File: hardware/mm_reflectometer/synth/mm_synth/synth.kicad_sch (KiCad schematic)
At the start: 44 parts

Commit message: adding bias circuitry to mm synth
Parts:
- added C?: 100 nF, symbol Device:C_Small
- added R?: 47k, symbol Device:R_Small
- FB? (x6): value FerriteBead_Small -> BLM15GG471SZ1D
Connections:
- net GND: now also C?.1
- net at C?.1, R?.2: now also U?.14 (CPout)
- net at U?.43 (Vtune): now also R?.1, R?.2
- new net VT_UNBUF: C?.2, R?.1
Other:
- note added: "TODO: CHECK CURRENTS, MAX 200 MA/FERRITE"
- moved on the sheet: C?, R?

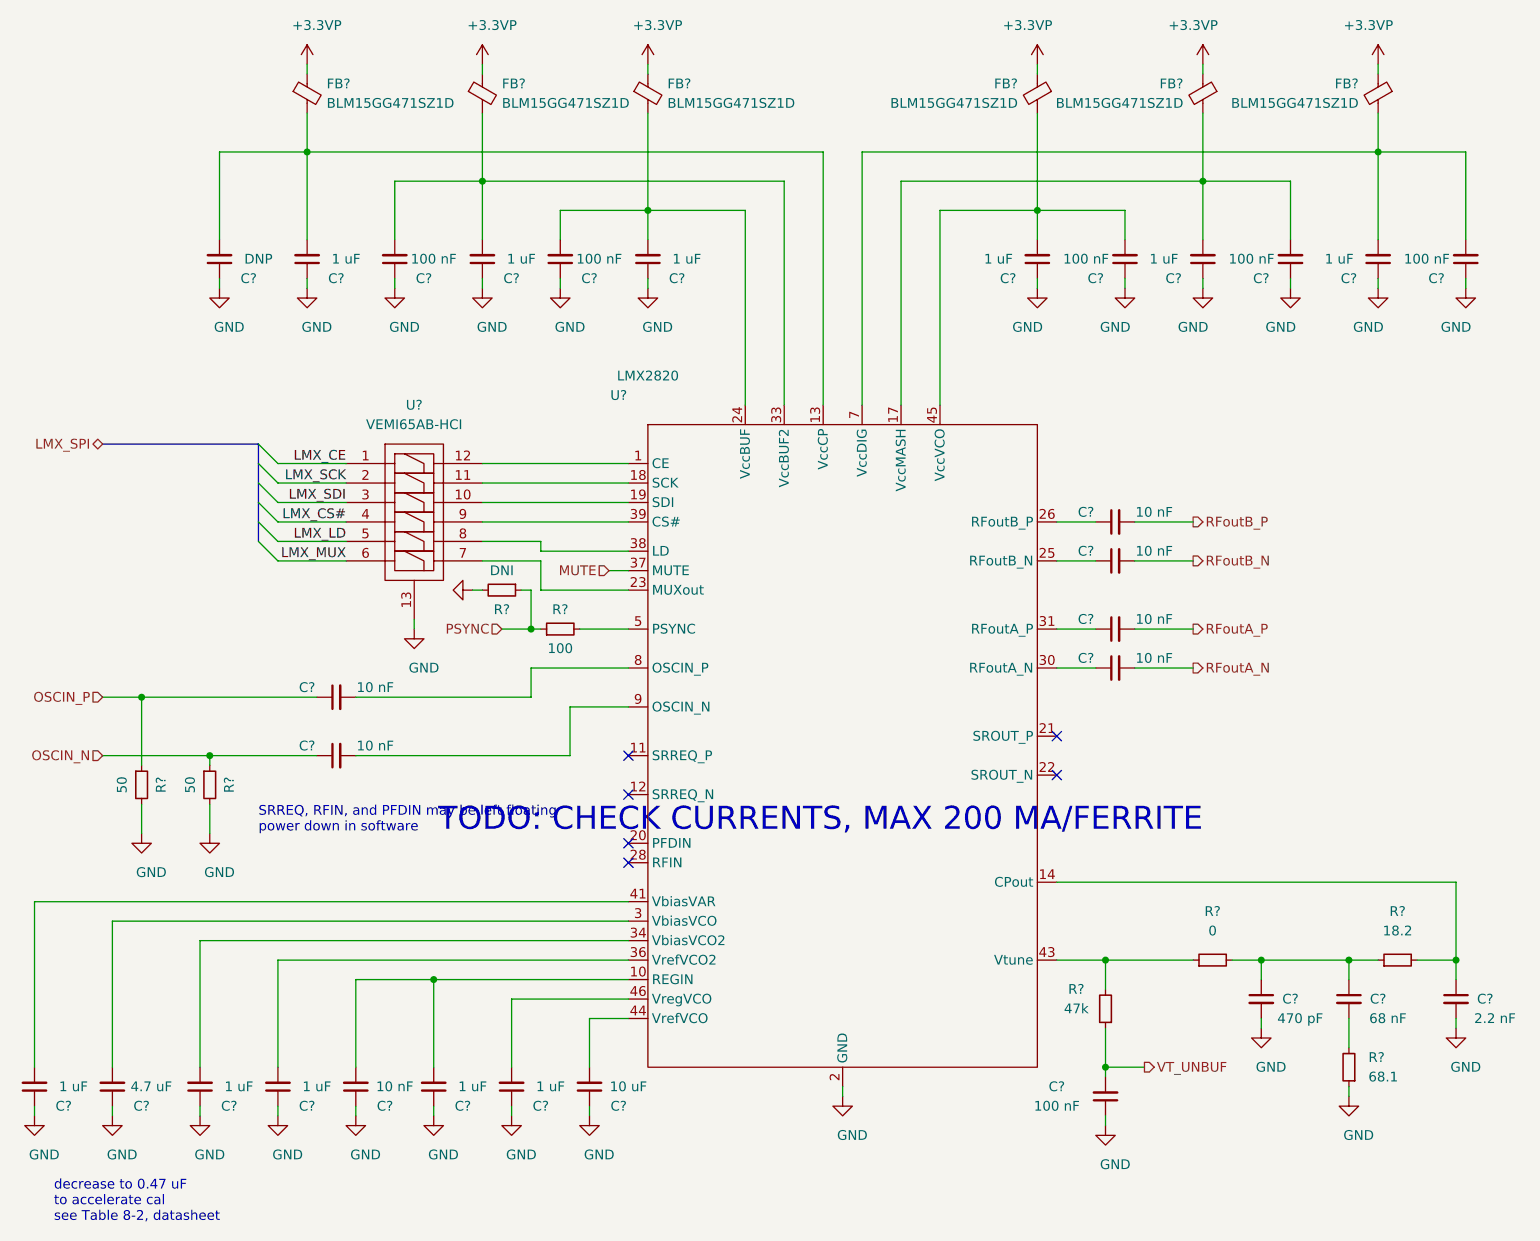
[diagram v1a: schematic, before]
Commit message: schematic work on mm synth -- starting voltage regulation
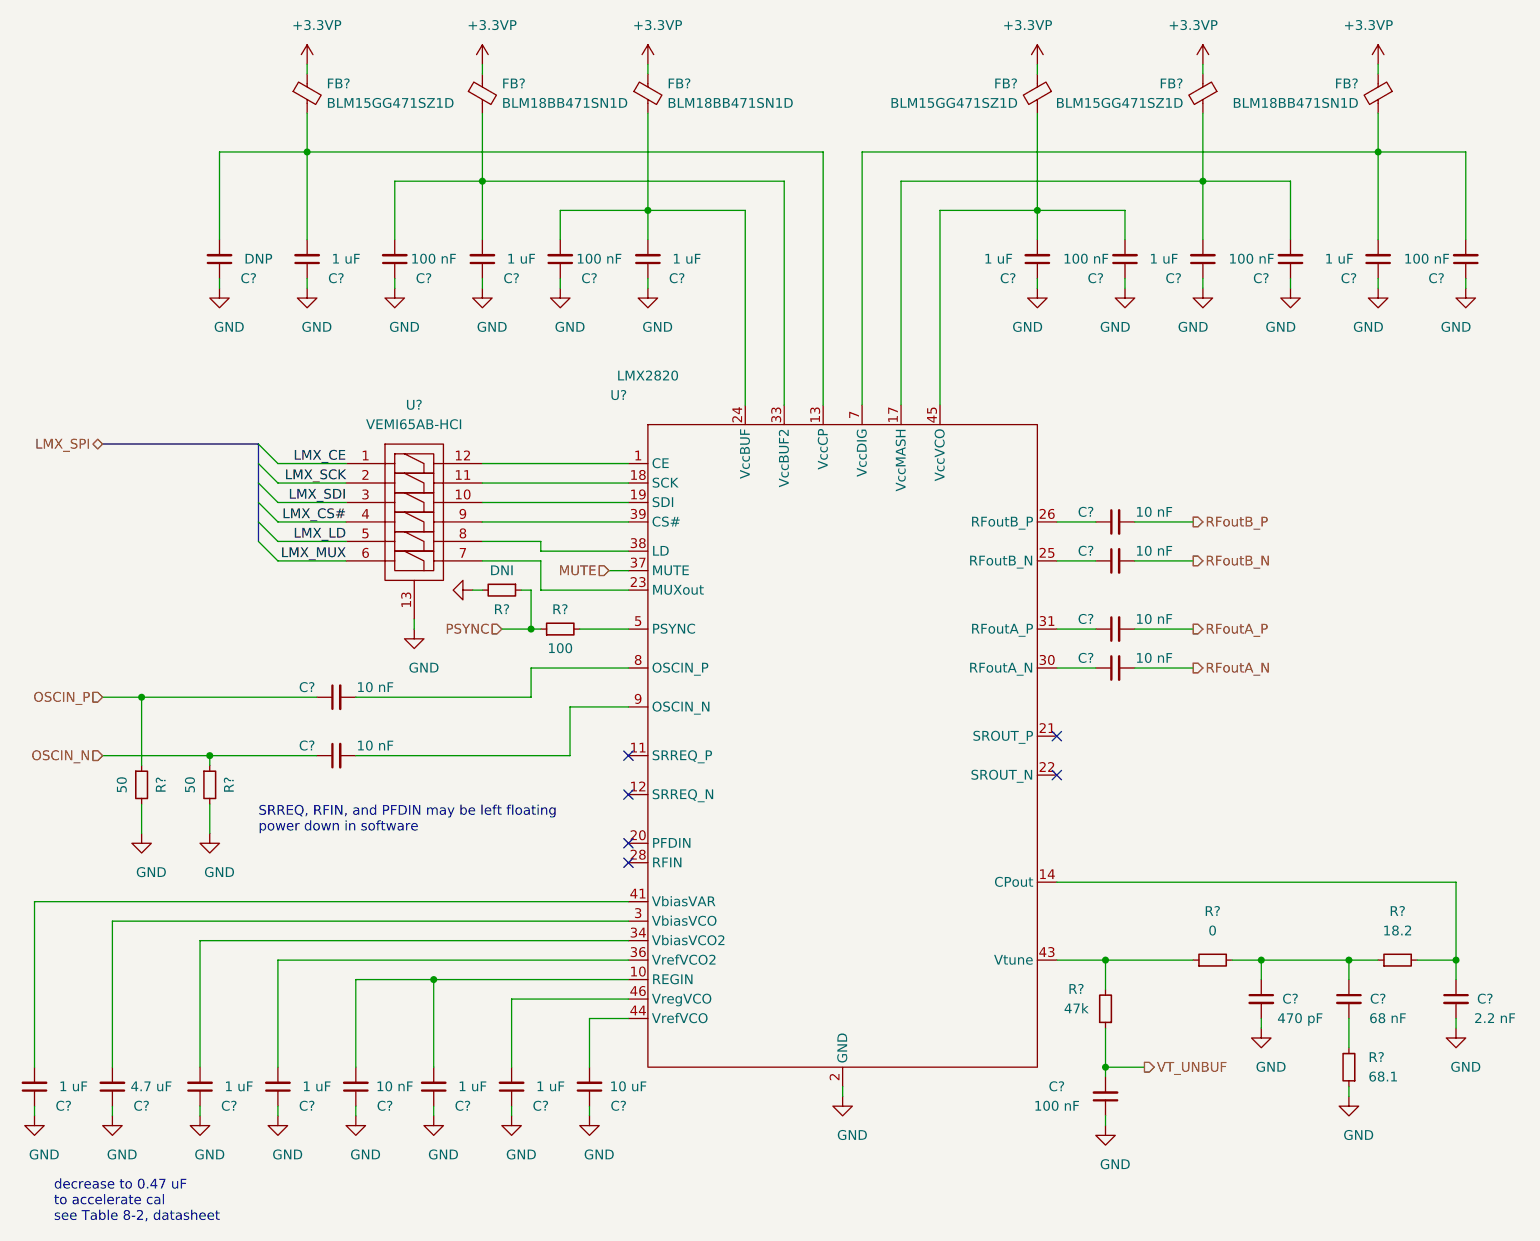
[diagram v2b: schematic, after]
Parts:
- FB? (x3): value BLM15GG471SZ1D -> BLM18BB471SN1D
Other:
- note removed: "TODO: CHECK CURRENTS, MAX 200 MA/FERRITE"
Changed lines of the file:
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@@
-(kicad_sch (version 20210126) (generator eeschema)
+(kicad_sch (version 20210406) (generator eeschema)
   (paper "A4")
   (junction (at 64.77 102.87) (diameter 0.9144) (color 0 0 0 0))
@@
     (stroke (width 0) (type solid) (color 0 0 0 0))
   )
-  (bus (pts (xy 80.01 72.39) (xy 80.01 69.85))
-    (stroke (width 0) (type solid) (color 0 0 0 0))
-  )
-  (bus (pts (xy 80.01 74.93) (xy 80.01 72.39))
-    (stroke (width 0) (type solid) (color 0 0 0 0))
-  )
-  (bus (pts (xy 80.01 77.47) (xy 80.01 74.93))
-    (stroke (width 0) (type solid) (color 0 0 0 0))
-  )
-  (bus (pts (xy 80.01 80.01) (xy 80.01 77.47))
-    (stroke (width 0) (type solid) (color 0 0 0 0))
-  )
-  (bus (pts (xy 80.01 82.55) (xy 80.01 80.01))
+  (bus (pts (xy 80.01 69.85) (xy 80.01 82.55))
     (stroke (width 0) (type solid) (color 0 0 0 0))
   )
@@
     (effects (font (size 1.27 1.27)) (justify left bottom))
   )
-  (text "TODO: CHECK CURRENTS, MAX 200 MA/FERRITE" (at 203.2 120.65 180)
-    (effects (font (size 3 3)) (justify right bottom))
-  )
   (label "LMX_CE" (at 91.44 72.39 180)
     (effects (font (size 1.27 1.27)) (justify right bottom))
@@
       (effects (font (size 1.27 1.27)) (justify left))
     )
-    (property "Value" "BLM15GG471SZ1D" (id 1) (at 111.76 25.4 0)
+    (property "Value" "BLM18BB471SN1D" (id 1) (at 111.76 25.4 0)
       (effects (font (size 1.27 1.27)) (justify left))
     )
@@
       (effects (font (size 1.27 1.27)) (justify left))
     )
-    (property "Value" "BLM15GG471SZ1D" (id 1) (at 133.35 25.4 0)
+    (property "Value" "BLM18BB471SN1D" (id 1) (at 133.35 25.4 0)
       (effects (font (size 1.27 1.27)) (justify left))
     )
@@
       (effects (font (size 1.27 1.27)) (justify left))
     )
-    (property "Value" "BLM15GG471SZ1D" (id 1) (at 223.52 25.4 0)
+    (property "Value" "BLM18BB471SN1D" (id 1) (at 223.52 25.4 0)
       (effects (font (size 1.27 1.27)) (justify left))
     )

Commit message: work on mm synth schematic - control signals and footprint assignments
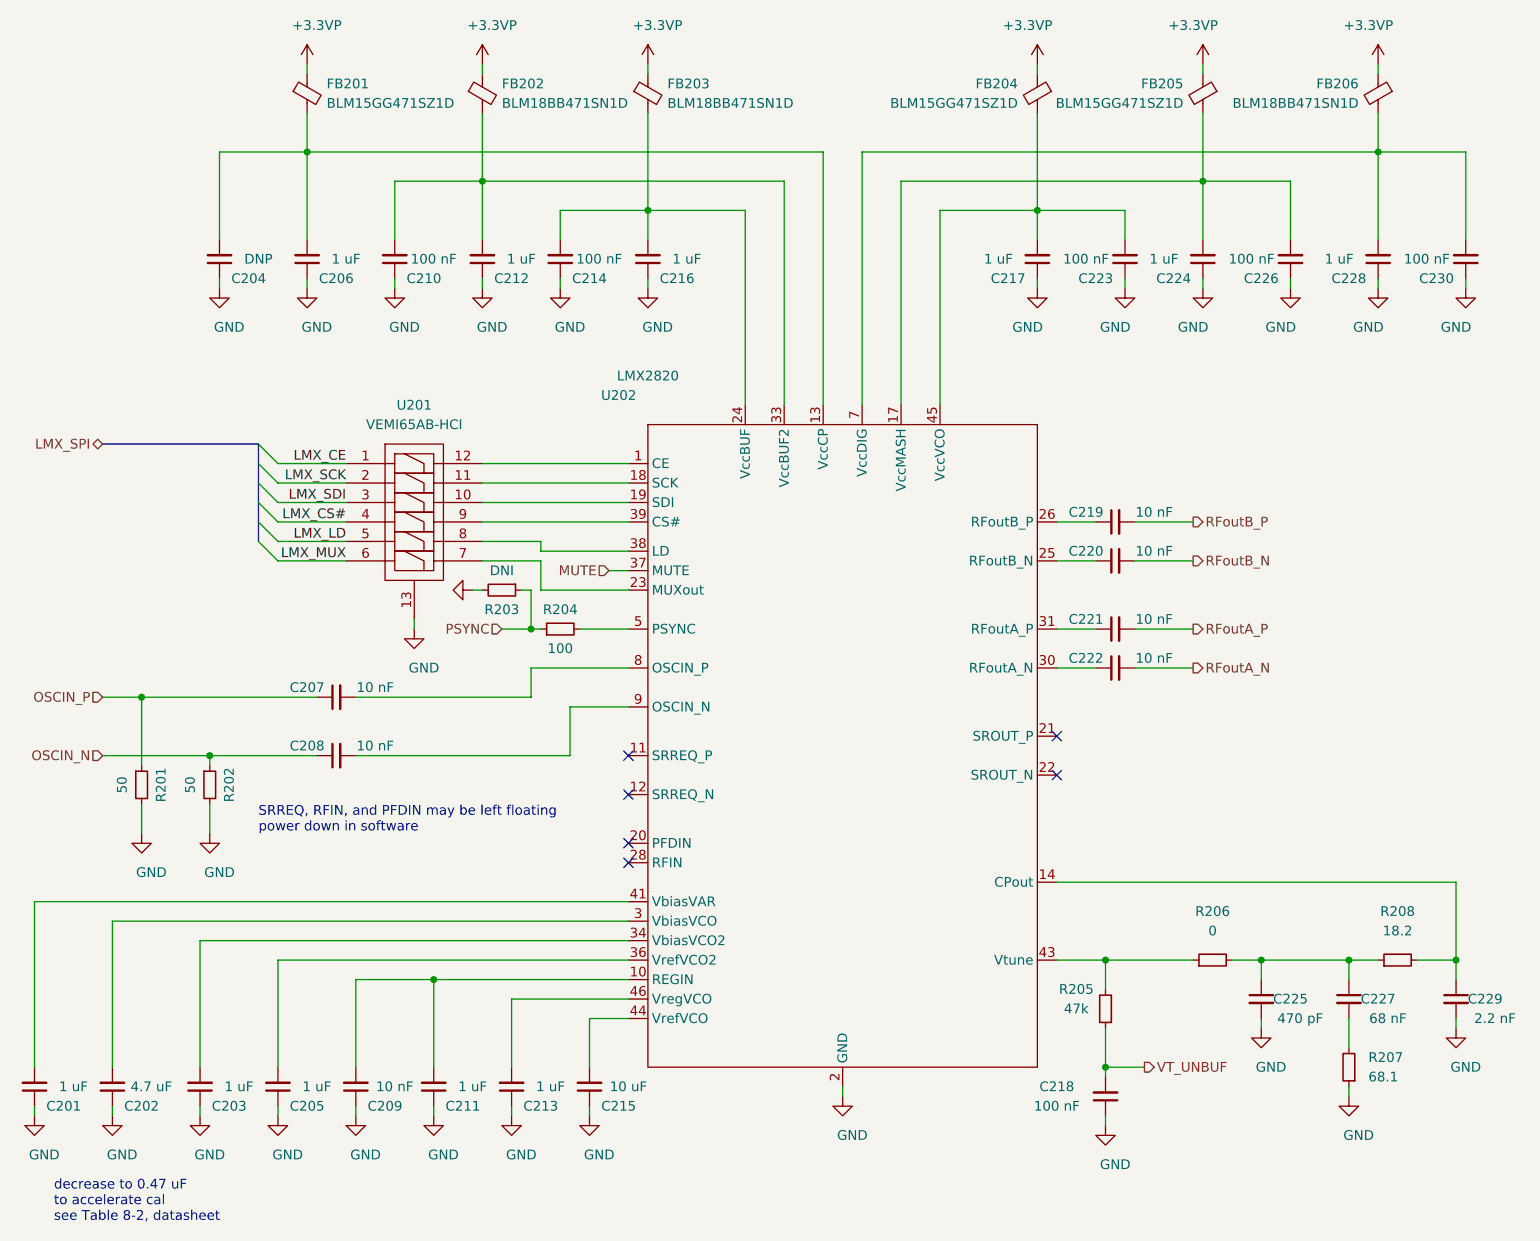
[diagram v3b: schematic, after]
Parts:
- C201, C203, C204, C205, C206, C207, C208, C209, C210, C211, C212, C213, C214, C216, C217, C219, C220, C221, C222, C223, C224, C226, C228, C230: renamed from C?; footprint (none) -> Capacitor_SMD:C_0402_1005Metric
- C202, C215, C218, C225, C227, C229: renamed from C?; footprint (none) -> Capacitor_SMD:C_0603_1608Metric
- R201, R202, R203, R204: renamed from R?; footprint (none) -> Resistor_SMD:R_0402_1005Metric
- R205, R206, R207, R208: renamed from R?; footprint (none) -> Resistor_SMD:R_0603_1608Metric
- U201: renamed from U?; footprint (none) -> vna_mm:LLP2513-13L
- gave numbers to parts that had none: 7

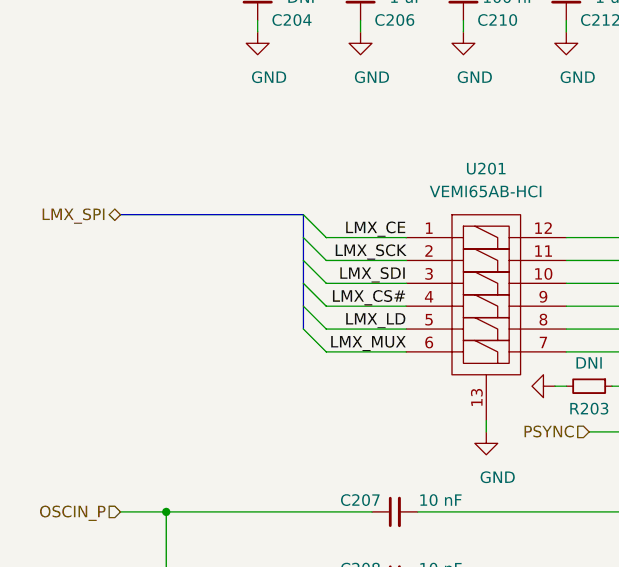
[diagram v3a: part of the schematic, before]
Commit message: added aux high speed io connector, fixed hierarchical buses
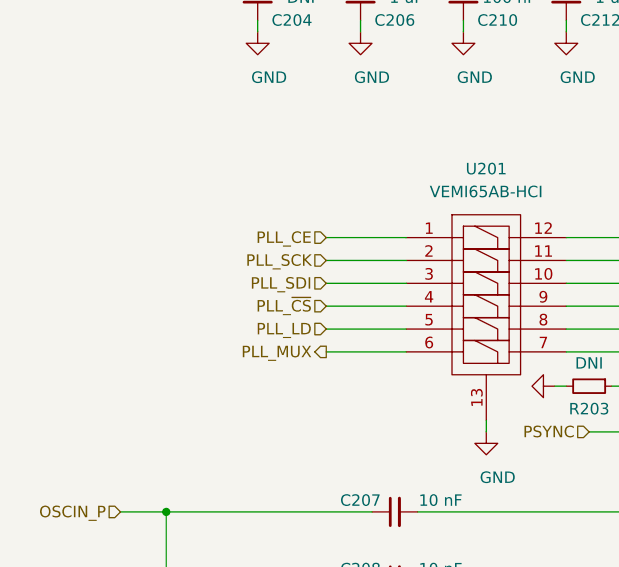
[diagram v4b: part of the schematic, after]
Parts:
- FB201, FB204, FB205: footprint (none) -> Inductor_SMD:L_0402_1005Metric
- FB202, FB203, FB206: footprint (none) -> Inductor_SMD:L_0603_1608Metric
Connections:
- net LMX_CE renamed PLL_CE
- net LMX_CS# renamed PLL_~{CS}
- net LMX_LD renamed PLL_LD
- net LMX_MUX renamed PLL_MUX
- net LMX_SCK renamed PLL_SCK
- net LMX_SDI renamed PLL_SDI
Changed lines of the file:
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@@
   (no_connect (at 184.15 107.95))
   (no_connect (at 184.15 113.03))
-  (bus_entry (at 80.01 69.85) (size 2.54 2.54)
-    (stroke (width 0.1524) (type solid) (color 0 0 0 0))
-  )
-  (bus_entry (at 80.01 72.39) (size 2.54 2.54)
-    (stroke (width 0.1524) (type solid) (color 0 0 0 0))
-  )
-  (bus_entry (at 80.01 74.93) (size 2.54 2.54)
-    (stroke (width 0.1524) (type solid) (color 0 0 0 0))
-  )
-  (bus_entry (at 80.01 77.47) (size 2.54 2.54)
-    (stroke (width 0.1524) (type solid) (color 0 0 0 0))
-  )
-  (bus_entry (at 80.01 80.01) (size 2.54 2.54)
-    (stroke (width 0.1524) (type solid) (color 0 0 0 0))
-  )
-  (bus_entry (at 80.01 82.55) (size 2.54 2.54)
-    (stroke (width 0.1524) (type solid) (color 0 0 0 0))
-  )
   (wire (pts (xy 50.8 129.54) (xy 50.8 151.13))
     (stroke (width 0) (type solid) (color 0 0 0 0))
@@
   )
   (wire (pts (xy 237.49 48.26) (xy 237.49 49.53))
-    (stroke (width 0) (type solid) (color 0 0 0 0))
-  )
-  (bus (pts (xy 59.69 69.85) (xy 80.01 69.85))
-    (stroke (width 0) (type solid) (color 0 0 0 0))
-  )
-  (bus (pts (xy 80.01 69.85) (xy 80.01 82.55))
     (stroke (width 0) (type solid) (color 0 0 0 0))
   )
@@
     (effects (font (size 1.27 1.27)) (justify left bottom))
   )
-  (label "LMX_CE" (at 91.44 72.39 180)
-    (effects (font (size 1.27 1.27)) (justify right bottom))
-  )
-  (label "LMX_SCK" (at 91.44 74.93 180)
-    (effects (font (size 1.27 1.27)) (justify right bottom))
-  )
-  (label "LMX_SDI" (at 91.44 77.47 180)
-    (effects (font (size 1.27 1.27)) (justify right bottom))
-  )
-  (label "LMX_CS#" (at 91.44 80.01 180)
-    (effects (font (size 1.27 1.27)) (justify right bottom))
-  )
-  (label "LMX_LD" (at 91.44 82.55 180)
-    (effects (font (size 1.27 1.27)) (justify right bottom))
-  )
-  (label "LMX_MUX" (at 91.44 85.09 180)
-    (effects (font (size 1.27 1.27)) (justify right bottom))
-  )
-  (hierarchical_label "LMX_SPI" (shape bidirectional) (at 59.69 69.85 180)
-    (effects (font (size 1.27 1.27)) (justify right))
-  )
   (hierarchical_label "OSCIN_P" (shape input) (at 59.69 102.87 180)
     (effects (font (size 1.27 1.27)) (justify right))
   )
   (hierarchical_label "OSCIN_N" (shape input) (at 59.69 110.49 180)
+    (effects (font (size 1.27 1.27)) (justify right))
+  )
+  (hierarchical_label "PLL_CE" (shape input) (at 82.55 72.39 180)
+    (effects (font (size 1.27 1.27)) (justify right))
+  )
+  (hierarchical_label "PLL_SCK" (shape input) (at 82.55 74.93 180)
+    (effects (font (size 1.27 1.27)) (justify right))
+  )
+  (hierarchical_label "PLL_SDI" (shape input) (at 82.55 77.47 180)
+    (effects (font (size 1.27 1.27)) (justify right))
+  )
+  (hierarchical_label "PLL_~{CS}" (shape input) (at 82.55 80.01 180)
+    (effects (font (size 1.27 1.27)) (justify right))
+  )
+  (hierarchical_label "PLL_LD" (shape input) (at 82.55 82.55 180)
+    (effects (font (size 1.27 1.27)) (justify right))
+  )
+  (hierarchical_label "PLL_MUX" (shape output) (at 82.55 85.09 180)
     (effects (font (size 1.27 1.27)) (justify right))
   )
@@
       (effects (font (size 1.27 1.27)) (justify left))
     )
-    (property "Footprint" "" (id 2) (at 84.582 24.13 90)
+    (property "Footprint" "Inductor_SMD:L_0402_1005Metric" (id 2) (at 84.582 24.13 90)
       (effects (font (size 1.27 1.27)) hide)
     )
@@
       (effects (font (size 1.27 1.27)) (justify left))
     )
-    (property "Footprint" "" (id 2) (at 107.442 24.13 90)
+    (property "Footprint" "Inductor_SMD:L_0603_1608Metric" (id 2) (at 107.442 24.13 90)
       (effects (font (size 1.27 1.27)) hide)
     )
@@
       (effects (font (size 1.27 1.27)) (justify left))
     )
-    (property "Footprint" "" (id 2) (at 129.032 24.13 90)
+    (property "Footprint" "Inductor_SMD:L_0603_1608Metric" (id 2) (at 129.032 24.13 90)
       (effects (font (size 1.27 1.27)) hide)
     )
@@
       (effects (font (size 1.27 1.27)) (justify left))
     )
-    (property "Footprint" "" (id 2) (at 183.388 24.13 90)
+    (property "Footprint" "Inductor_SMD:L_0402_1005Metric" (id 2) (at 183.388 24.13 90)
       (effects (font (size 1.27 1.27)) hide)
     )
@@
       (effects (font (size 1.27 1.27)) (justify left))
     )
-    (property "Footprint" "" (id 2) (at 204.978 24.13 90)
+    (property "Footprint" "Inductor_SMD:L_0402_1005Metric" (id 2) (at 204.978 24.13 90)
       (effects (font (size 1.27 1.27)) hide)
     )
@@
       (effects (font (size 1.27 1.27)) (justify left))
     )
-    (property "Footprint" "" (id 2) (at 227.838 24.13 90)
-      (effects (font (size 1.27 1.27)) hide)
-    )
+    (property "Footprint" "Inductor_SMD:L_0603_1608Metric" (id 2) (at 227.838 24.13 90)
+      (effects (font (size 1.27 1.27)) hide)
+    )
